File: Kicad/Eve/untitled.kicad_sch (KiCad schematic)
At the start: 9 parts

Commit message: updtated Kicad ver 7.11.23
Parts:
- removed U2: ~, libs:LT1076CR-PBF, symbol custom:LT1076
- added D6: LED, LED_SMD:LED_0603_1608Metric_Pad1.05x0.95mm_HandSolder, symbol Device:LED
- added R7: 1k, Resistor_SMD:R_0603_1608Metric_Pad0.98x0.95mm_HandSolder, symbol Device:R_Small
- added U1: LT1076, symbol custom:LT1076
- CR1: footprint libs:DST10100S -> TO277B_LTF
- R9: value 5k -> 5.1k
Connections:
- net +3.3V: now also R7.1
- net GND: now also D6.1 (K), U1.4 (GND)
- net Vsw: now also U1.2 (Vsw)
- net at R8.1: now also U1.6 (Vc)
- net at R10.1, R9.2: now also U1.5 (FB)
- net +24V renamed 24V
- net 24V: now also U1.1 (Vin), U1.7 (Shutdown)
- new net: D6.2 (A), R7.2
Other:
- moved on the sheet: L1, R10

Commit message: KiCad changes 10/11
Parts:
- removed C6: 220uF, Capacitor_SMD:CP_Elec_10x10.5, symbol Device:C_Polarized_Small
- removed C8: 470uF, Capacitor_SMD:CP_Elec_10x10.5, symbol Device:C_Polarized_Small
- removed CR1: DST10100S, TO277B_LTF, symbol 2023-03-19_11-33-54:DST10100S
- removed L1: 22uH, Inductor_SMD:L_Wuerth_WE-PD-Typ-LS_Handsoldering, symbol Device:L_Small
- removed R10: 10k, Resistor_SMD:R_0603_1608Metric_Pad0.98x0.95mm_HandSolder, symbol Device:R_Small
- removed R8: 2.7k, Resistor_SMD:R_0603_1608Metric_Pad0.98x0.95mm_HandSolder, symbol Device:R_Small
- removed R9: 5.1k, Resistor_SMD:R_0603_1608Metric_Pad0.98x0.95mm_HandSolder, symbol Device:R_Small
- removed U1: LT1076, symbol custom:LT1076
- added C8: 1u, Capacitor_SMD:C_0603_1608Metric_Pad1.08x0.95mm_HandSolder, symbol Device:C_Small
- added U1: BU33SD5WG-TR, Package_TO_SOT_SMD:SOT-23-5, symbol Regulator_Linear:MCP1802x-xx02xOT
- C7: value 10n -> 1u
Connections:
- net +3.3V: now also C8.1, U1.5 (VOUT)
- net GND: now also C8.2, U1.2 (GND)
- net +5V: now reaches C7.1
- net +5V: now also U1.1 (VIN), U1.3 (~{SHDN})
- no-connect marks 1 -> 0
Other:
- note removed: "Reference voltage : VFB = 2.21V"

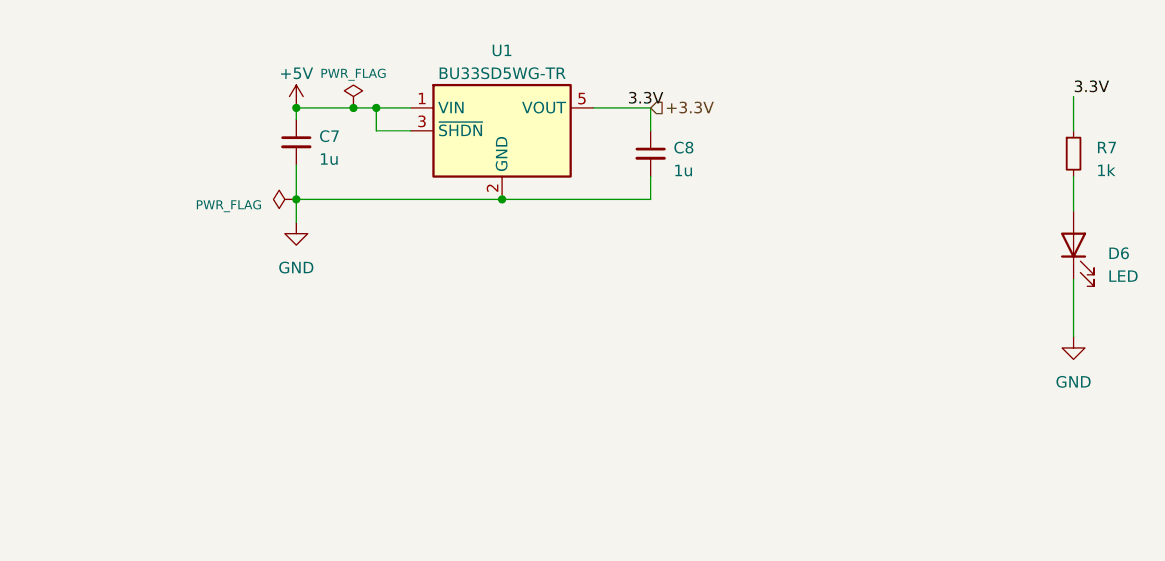
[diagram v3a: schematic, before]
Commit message: added Kicad libraries to git + sch changes 11/11/23
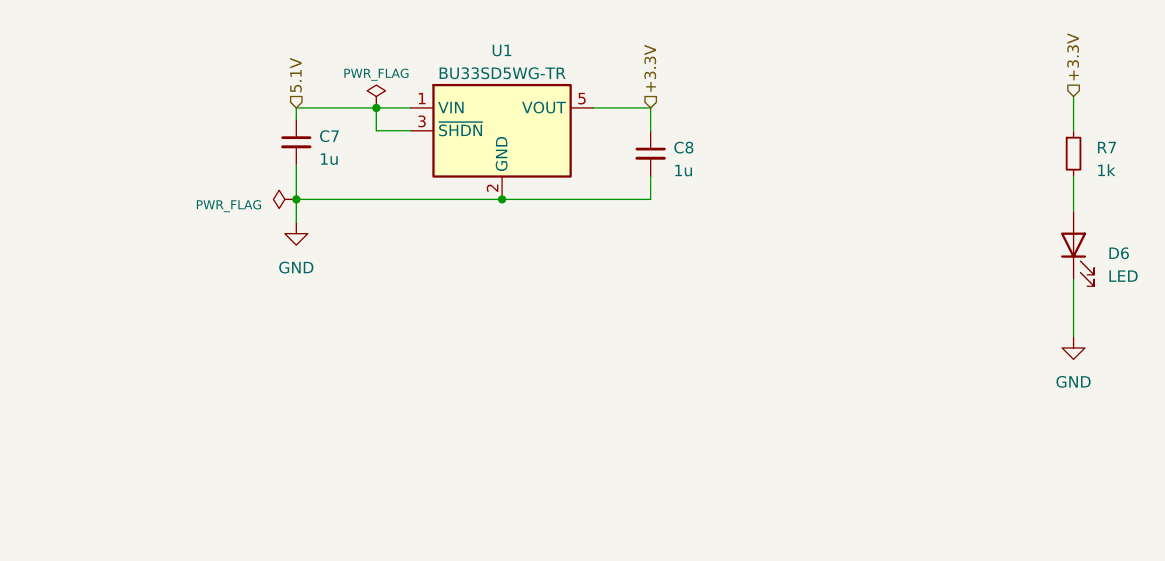
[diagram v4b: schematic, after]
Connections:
- net +5V renamed 5.1V
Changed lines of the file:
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@@
 (kicad_sch (version 20230121) (generator eeschema)
   (paper "A4")
-  (junction (at 123.19 72.39) (diameter 0) (color 0 0 0 0)
-  )
   (junction (at 146.05 82.55) (diameter 0) (color 0 0 0 0)
   )
-  (junction (at 129.54 72.39) (diameter 0) (color 0 0 0 0)
-  )
   (junction (at 132.08 72.39) (diameter 0) (color 0 0 0 0)
   )
@@
     (stroke (width 0) (type default))
   )
+  (wire (pts (xy 123.19 72.39) (xy 132.08 72.39))
+    (stroke (width 0) (type default))
+  )
   (wire (pts (xy 209.55 80.01) (xy 209.55 83.82))
     (stroke (width 0) (type default))
@@
     (stroke (width 0) (type default))
   )
-  (wire (pts (xy 129.54 72.39) (xy 123.19 72.39))
-    (stroke (width 0) (type default))
-  )
   (wire (pts (xy 162.56 72.39) (xy 156.21 72.39))
     (stroke (width 0) (type default))
   )
-  (wire (pts (xy 132.08 72.39) (xy 129.54 72.39))
-    (stroke (width 0) (type default))
-  )
   (wire (pts (xy 123.19 82.55) (xy 146.05 82.55))
     (stroke (width 0) (type default))
@@
     (stroke (width 0) (type default))
   )
-  (label "3.3V" (at 209.55 71.12 0) (fields_autoplaced)
-    (effects (font (size 1.27 1.27)) (justify left bottom))
-  )
-  (label "3.3V" (at 160.02 72.39 0) (fields_autoplaced)
-    (effects (font (size 1.27 1.27)) (justify left bottom))
-  )
-  (hierarchical_label "+3.3V" (shape input) (at 162.56 72.39 0) (fields_autoplaced)
+  (hierarchical_label "+3.3V" (shape input) (at 209.55 71.12 90) (fields_autoplaced)
+    (effects (font (size 1.27 1.27)) (justify left))
+  )
+  (hierarchical_label "5.1V" (shape input) (at 123.19 72.39 90) (fields_autoplaced)
+    (effects (font (size 1.27 1.27)) (justify left))
+  )
+  (hierarchical_label "+3.3V" (shape input) (at 162.56 72.39 90) (fields_autoplaced)
     (effects (font (size 1.27 1.27)) (justify left))
   )
@@
     )
   )
-  (symbol (lib_id "power:+5V") (at 123.19 72.39 0) (unit 1)
-    (in_bom yes) (on_board yes) (dnp no) (fields_autoplaced)
-    (property "Reference" "#PWR031" (at 123.19 76.2 0)
-      (effects (font (size 1.27 1.27)) hide)
-    )
-    (property "Value" "+5V" (at 123.19 68.58 0)
-      (effects (font (size 1.27 1.27)))
-    )
-    (property "Footprint" "" (at 123.19 72.39 0)
-      (effects (font (size 1.27 1.27)) hide)
-    )
-    (property "Datasheet" "" (at 123.19 72.39 0)
-      (effects (font (size 1.27 1.27)) hide)
-    )
-    (pin "1")
-    (instances
-      (project "Robourt"
-        (path "/87ede840-4957-4951-b25a-c132e7988ddc/45a40ff7-b6ec-4165-9635-bd80258dd043"
-          (reference "#PWR031") (unit 1)
-        )
-      )
-    )
-  )
-  (symbol (lib_id "power:PWR_FLAG") (at 129.54 72.39 0) (unit 1)
-    (in_bom yes) (on_board yes) (dnp no) (fields_autoplaced)
-    (property "Reference" "#FLG01" (at 129.54 70.485 0)
-      (effects (font (size 1.27 1.27)) hide)
-    )
-    (property "Value" "PWR_FLAG" (at 129.54 68.58 0)
+  (symbol (lib_id "power:PWR_FLAG") (at 132.08 72.39 0) (unit 1)
+    (in_bom yes) (on_board yes) (dnp no) (fields_autoplaced)
+    (property "Reference" "#FLG01" (at 132.08 70.485 0)
+      (effects (font (size 1.27 1.27)) hide)
+    )
+    (property "Value" "PWR_FLAG" (at 132.08 68.58 0)
       (effects (font (size 1 1)))
     )
-    (property "Footprint" "" (at 129.54 72.39 0)
-      (effects (font (size 1.27 1.27)) hide)
-    )
-    (property "Datasheet" "~" (at 129.54 72.39 0)
-      (effects (font (size 1.27 1.27)) hide)
-    )
+    (property "Footprint" "" (at 132.08 72.39 0)
+      (effects (font (size 1.27 1.27)) hide)
+    )
+    (property "Datasheet" "~" (at 132.08 72.39 0)
+      (effects (font (size 1.27 1.27)) hide)
+    )
